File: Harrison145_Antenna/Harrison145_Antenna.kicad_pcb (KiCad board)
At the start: 2 copper layers, 240.3 x 138.3 mm, 12 parts, among them J1 Conn_01x01, J2 Conn_01x01, J3 AudioJack3, SW1 SW_SPDT

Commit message: Antenna design changes
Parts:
- removed AE2: Antenna, Theremin:PlateAntenna
- RV1: value R_Potentiometer_MountingPin -> R_Potentiometer_US
- moved SW1 89.5 mm to (181.7, 55.2), turned to 180 degrees
- moved H2 87.4 mm to (195.0, 61.5), turned to -90 degrees
- moved H1 87.4 mm to (156.0, 61.5), turned to -90 degrees
- moved J2 68.8 mm to (182.0, 71.9), turned to 180 degrees
- moved J1 68.8 mm to (169.0, 71.9), turned to 180 degrees
- moved J3 66.2 mm to (197.8, 79.1), turned to -90 degrees
- moved H5 43.9 mm to (195.0, 96.0), turned to -90 degrees
- moved BT1 31.4 mm to (175.5, 100.0), turned to 0 degrees
- moved H3 31.2 mm to (195.0, 130.5), turned to -90 degrees
- moved H4 31.2 mm to (156.0, 130.5), turned to -90 degrees
- moved RV1 24.4 mm to (193.9, 113.2), turned to 90 degrees
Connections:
- net Net-(AE1-Pad1) renamed /PITCH_ANT
- net Net-(H4-Pad1) renamed /VOL_ANT
- H2 pad 1: Net-(H2-Pad1) -> Net-(SW1-A)
- RV1 pad 1: Net-(H3-Pad1) -> GND
- RV1 pad 3: GND -> Net-(H3-Pad1)
- SW1 pad 1: unconnected-(SW1-Pad1) -> Net-(SW1-A)
- SW1 pad 3: Net-(H2-Pad1) -> unconnected-(SW1-C-Pad3)
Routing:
- net Net-(J3-PadR): track 0.00 -> 44.5 mm, vias 0 -> 1
- net Net-(BT1-+): track 0.00 -> 29.0 mm
- net Net-(H3-Pad1): track 0.00 -> 24.1 mm
- net Net-(SW1-A): track 0.00 -> 11.6 mm
- added copper zone on F.Cu, net /VOL_ANT
- added copper zone on B.Cu, net GND
- added copper zone on F.Cu, net GND
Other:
- board size 240.3 x 138.3 mm -> 170.3 x 101.1 mm

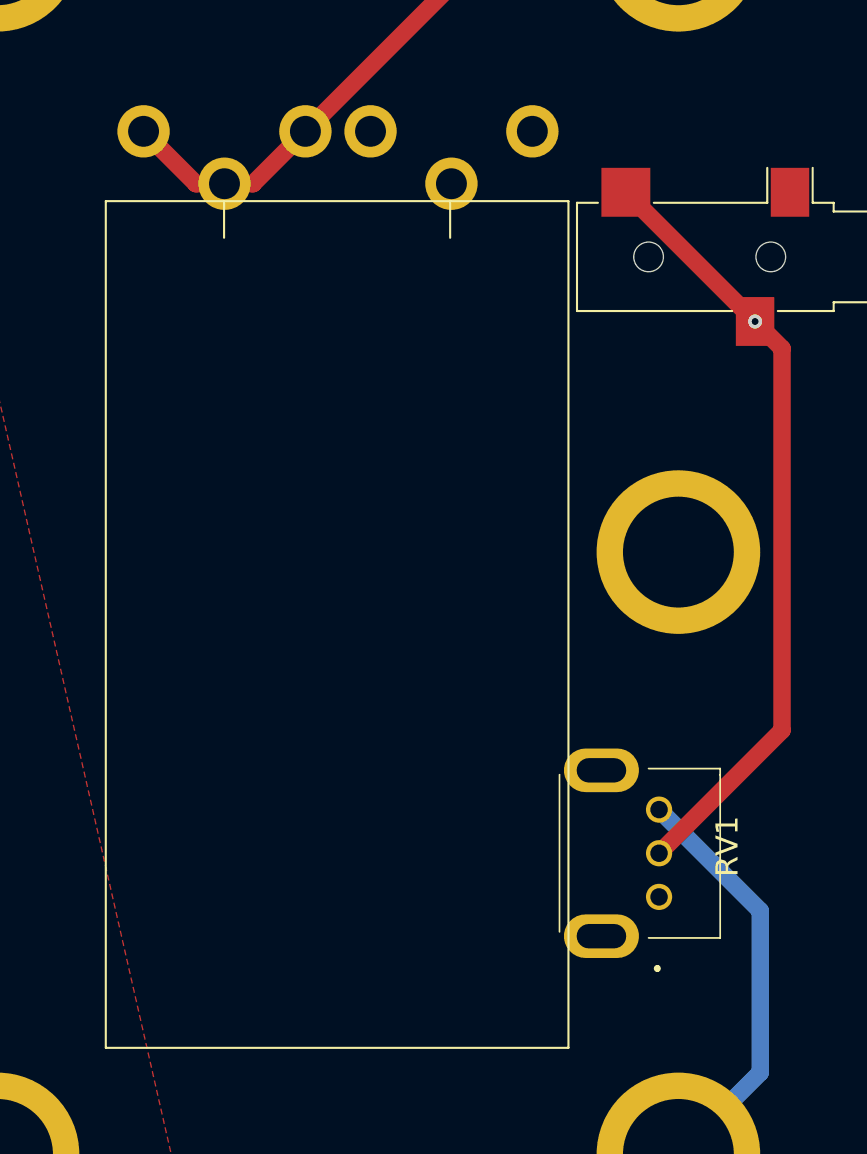
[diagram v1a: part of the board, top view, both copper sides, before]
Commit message: Combine 9V battery and terminals into a single footprint
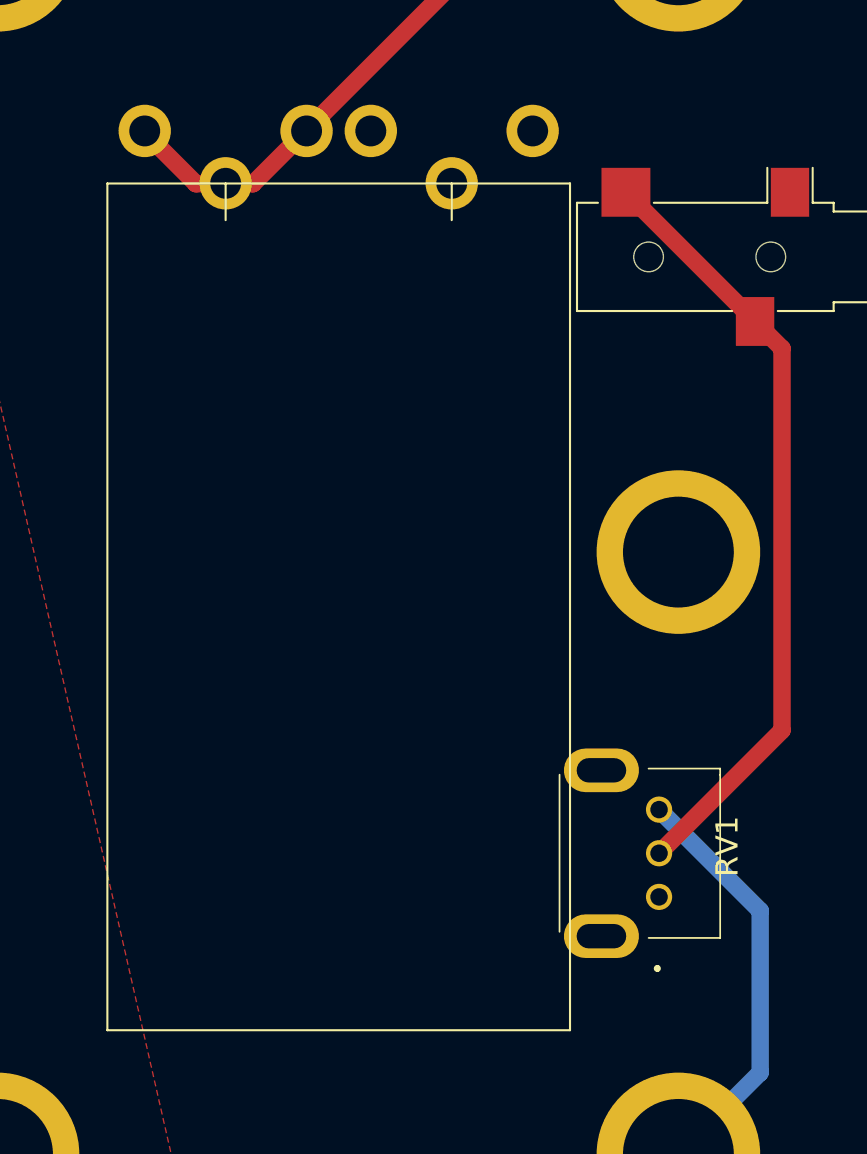
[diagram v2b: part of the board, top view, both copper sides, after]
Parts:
- removed J1: Conn_01x01, Theremin:Keystone_594
- removed J2: Conn_01x01, Theremin:Keystone_593
- moved BT1 1.01 mm to (175.6, 99.0)
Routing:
- net Net-(J3-PadR): vias 1 -> 0

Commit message: 'Interference pattern' antenna design
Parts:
- moved J3 62.2 mm to (260.0, 77.5), turned to -45 degrees
- moved H2 57.2 mm to (252.2, 59.9)
- moved SW1 57.2 mm to (238.9, 53.6)
- moved BT1 57.2 mm to (232.8, 97.4)
- moved H1 57.2 mm to (213.2, 59.9)
- moved H3 57.2 mm to (252.2, 128.9)
- moved H4 57.2 mm to (213.2, 128.9)
- moved H5 57.2 mm to (252.2, 94.4)
- moved RV1 57.2 mm to (251.1, 111.6)
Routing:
- net /VOL_ANT: track 0.00 -> 68.0 mm
- net Net-(BT1-+): track 29.0 -> 11.4 mm
- net Net-(SW1-A): track 11.6 -> 0.00 mm
- net Net-(J3-PadR): track 44.5 -> 55.6 mm
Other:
- board size 170.3 x 101.1 mm -> 343 x 157.2 mm

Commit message: Added step files for full antenna assembly
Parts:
- added REF**: TopBoardModels, Theremin:TopBoardModels, F.Cu at (213.2, 59.9)
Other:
- outline, holes or cut-outs redrawn
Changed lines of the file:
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@@
+    )
+  )
+  (footprint "Theremin:TopBoardModels" (layer "F.Cu")
+    (at 213.24817 59.873409 -90)
+    (fp_text reference "REF**" (at 0 -0.5 -90 unlocked) (layer "F.SilkS") hide
+        (effects (font (size 1 1) (thickness 0.15)))
+    )
+    (fp_text value "TopBoardModels" (at 0 1 -90 unlocked) (layer "F.Fab") hide
+        (effects (font (size 1 1) (thickness 0.15)))
+    )
+    (fp_text user "${REFERENCE}" (at 0 2.5 -90 unlocked) (layer "F.Fab") hide
+        (effects (font (size 1 1) (thickness 0.15)))
+    )
+    (fp_circle (center 0 -39) (end 5.5 -39)
+      (stroke (width 0.12) (type default)) (fill none) (layer "F.SilkS"))
+    (fp_circle (center 0 0) (end 5.5 0)
+      (stroke (width 0.12) (type default)) (fill none) (layer "F.SilkS"))
+    (fp_circle (center 34.5 -39) (end 40 -39)
+      (stroke (width 0.12) (type default)) (fill none) (layer "F.SilkS"))
+    (fp_circle (center 69 -39) (end 74.5 -39)
+      (stroke (width 0.12) (type default)) (fill none) (layer "F.SilkS"))
+    (fp_circle (center 69 0) (end 74.5 0)
+      (stroke (width 0.12) (type default)) (fill none) (layer "F.SilkS"))
+    (model "${KIPRJMOD}/Libraries/Theremin.pretty/m4_15mm.stp"
+      (offset (xyz 0 0 10))
+      (scale (xyz 1 1 1))
+      (rotate (xyz 90 180 90))
+    )
+    (model "${KIPRJMOD}/Libraries/Theremin.pretty/m4_15mm.stp"
+      (offset (xyz 34.5 39 10))
+      (scale (xyz 1 1 1))
+      (rotate (xyz 90 180 90))
+    )
+    (model "${KIPRJMOD}/Libraries/Theremin.pretty/m4_15mm.stp"
+      (offset (xyz 0 39 10))
+      (scale (xyz 1 1 1))
+      (rotate (xyz 90 180 90))
+    )
+    (model "${KIPRJMOD}/Libraries/Theremin.pretty/m4_15mm.stp"
+      (offset (xyz 69 39 10))
+      (scale (xyz 1 1 1))
+      (rotate (xyz 90 180 90))
+    )
+    (model "${KIPRJMOD}/Libraries/Theremin.pretty/m4_15mm.stp"
+      (offset (xyz 69 0 10))
+      (scale (xyz 1 1 1))
+      (rotate (xyz 90 180 90))
+    )
+    (model "${KIPRJMOD}/Libraries/Theremin.pretty/Harrison145.step"
+      (offset (xyz -148.5 99 19))
+      (scale (xyz 1 1 1))
+      (rotate (xyz 0 0 0))
+    )
+    (model "${KIPRJMOD}/Libraries/Theremin.pretty/m4_10mm.stp"
+      (offset (xyz 34.5 39 24.5))
+      (scale (xyz 1 1 1))
+      (rotate (xyz 90 180 90))
+    )
+    (model "${KIPRJMOD}/Libraries/Theremin.pretty/cylinder-300mm.step"
+      (offset (xyz 34.5 39 30))
+      (scale (xyz 1 1 1))
+      (rotate (xyz 0 0 0))
+    )
+    (model "${KIPRJMOD}/Libraries/Theremin.pretty/m4_screw.step"
+      (offset (xyz 0 0 19))
+      (scale (xyz 1 1 1))
+      (rotate (xyz 0 0 0))
+    )
+    (model "${KIPRJMOD}/Libraries/Theremin.pretty/m4_screw.step"
+      (offset (xyz 69 39 19))
+      (scale (xyz 1 1 1))
+      (rotate (xyz 0 0 0))
+    )
+    (model "${KIPRJMOD}/Libraries/Theremin.pretty/m4_screw.step"
+      (offset (xyz 0 39 19))
+      (scale (xyz 1 1 1))
+      (rotate (xyz 0 0 0))
+    )
+    (model "${KIPRJMOD}/Libraries/Theremin.pretty/m4_screw.step"
+      (offset (xyz 69 0 19))
+      (scale (xyz 1 1 1))
+      (rotate (xyz 0 0 0))
     )
   )
@@
   (gr_line (start 272.295486 156.365) (end -60.695486 156.365)
     (stroke (width 0.1) (type default)) (layer "Edge.Cuts"))
+  (gr_circle (center 168.75 91) (end 176.6875 91)
+    (stroke (width 0.1) (type default)) (fill none) (layer "Edge.Cuts"))
   (gr_arc (start 273.874956 39.36116) (mid 276.351183 41.180868) (end 277.295486 44.105133)
     (stroke (width 0.1) (type default)) (layer "Edge.Cuts"))
@@
   (gr_line (start 273.874956 39.36116) (end 154.018984 -0.543972)
     (stroke (width 0.1) (type default)) (layer "Edge.Cuts"))
+  (dimension (type aligned) (layer "F.Cu")
+    (pts (xy 252.248171 59.873409) (xy 213.24817 59.873409))
+    (height 30.123409)
+    (gr_text "39.0000 mm" (at 232.748171 28.35) (layer "F.Cu")
+      (effects (font (size 1.2 1.2) (thickness 0.2)))
+    )
+    (format (prefix "") (suffix "") (units 3) (units_format 1) (precision 4))
+    (style (thickness 0.1) (arrow_length 1.27) (text_position_mode 0) (extension_height 0.58642) (extension_offset 0.5) keep_text_aligned)
+  )
+  (dimension (type aligned) (layer "F.Cu")
+    (pts (xy 252.248171 59.873409) (xy 252.248171 94.373406))
+    (height -30.751829)
+    (gr_text "34.5000 mm" (at 281.6 77.123407 90) (layer "F.Cu")
+      (effects (font (size 1.2 1.2) (thickness 0.2)))
+    )
+    (format (prefix "") (suffix "") (units 3) (units_format 1) (precision 4))
+    (style (thickness 0.1) (arrow_length 1.27) (text_position_mode 0) (extension_height 0.58642) (extension_offset 0.5) keep_text_aligned)
+  )
   (segment (start 252.248169 128.873408) (end 254.939158 126.182419) (width 0.8) (layer "F.Cu") (net 2))
   (segment (start 257.5 120) (end 257.5 117.74264) (width 0.8) (layer "F.Cu") (net 2))

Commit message: Remove kicad sims
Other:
- board text added: "To do: - Add TVS diode - Switch to SMT battery terminals - Change stackup"
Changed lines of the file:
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@@
   (gr_line (start 273.874956 39.36116) (end 154.018984 -0.543972)
     (stroke (width 0.1) (type default)) (layer "Edge.Cuts"))
+  (gr_text "To do:\n- Add TVS diode\n- Switch to SMT battery terminals\n- Change stackup" (at 155.25 36.25) (layer "Cmts.User")
+    (effects (font (size 2 2) (thickness 0.15)) (justify left bottom))
+  )
   (dimension (type aligned) (layer "F.Cu")
     (pts (xy 252.248171 59.873409) (xy 213.24817 59.873409))
@@
     (polygon
       (pts
-        (xy 200.6 148.4)
-        (xy 271.882827 148.4)
-        (xy 271.882827 42.9)
-        (xy 200.6 42.9)
+        (xy 198.35 145)
+        (xy 269.632827 145)
+        (xy 269.632827 39.5)
+        (xy 198.35 39.5)
       )
     )
@@
     (polygon
       (pts
-        (xy 200.7 148.4)
-        (xy 271.9 148.4)
-        (xy 271.9 42.9)
-        (xy 200.7 42.9)
+        (xy 198.45 145)
+        (xy 269.65 145)
+        (xy 269.65 39.5)
+        (xy 198.45 39.5)
       )
     )

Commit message: Cutouts on antenna pcb
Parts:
- added F1: Polyfuse_Small, Fuse:Fuse_1812_4532Metric_Pad1.30x3.40mm_HandSolder, F.Cu at (232.5, 66.5)
- moved SW1 6.49 mm to (232.8, 55.9)
- moved BT1 5.11 mm to (232.8, 102.5)
- moved J3 5.03 mm to (255.0, 78.0), turned to -90 degrees
- moved RV1 4.36 mm to (255.5, 111.6)
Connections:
- SW1 pad 2: Net-(BT1-+) -> Net-(SW1-B)
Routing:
- net Net-(J3-PadR): track 55.6 -> 0.00 mm
- net Net-(H3-Pad1): track 24.6 -> 0.00 mm
- net Net-(SW1-B): track 0.00 -> 5.86 mm
- net Net-(BT1-+): track 11.4 -> 6.39 mm
- removed copper zone on B.Cu, net GND
- removed copper zone on F.Cu, net GND
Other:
- board size 343 x 157.2 mm -> 322.5 x 110 mm
- board text added: "To do: - Add reverse polarity diode - Switch to SMT battery terminals"
- board text removed: "To do: - Add TVS diode - Switch to SMT battery terminals - Change stackup"
